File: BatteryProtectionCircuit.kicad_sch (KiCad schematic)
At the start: 0 parts

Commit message: Added initial power supply and wiring
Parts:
- added R1: R_US, symbol Device:R_US
- added U1: LMC555xN, Package_DIP:DIP-8_W7.62mm, symbol Timer:LMC555xN
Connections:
- new net: R1.2, U1.7 (DIS)
- new net +5V: U1.8 (VCC)

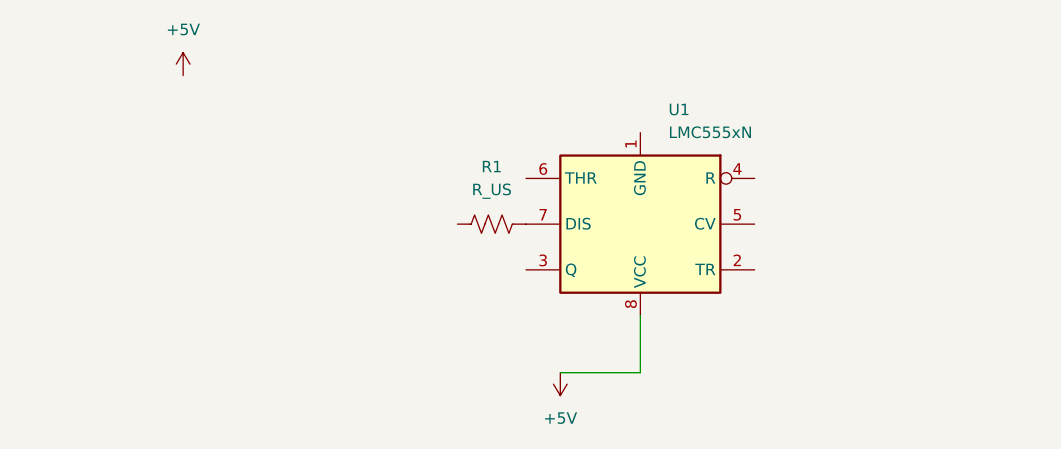
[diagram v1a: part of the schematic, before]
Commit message: BPC timer module complete (for 1 cell)
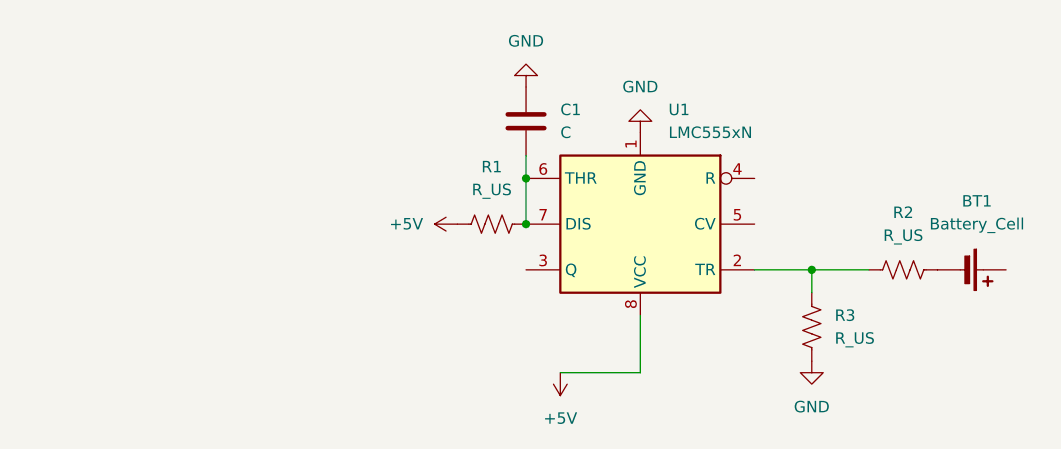
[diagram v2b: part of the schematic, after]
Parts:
- added BT1: Battery_Cell, symbol Device:Battery_Cell
- added C1: C, symbol Device:C
- added R2, R3: R_US, symbol Device:R_US
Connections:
- net +5V: now also R1.1
- net at R1.2, U1.7 (DIS): now also U1.6 (THR), C1.2
- net GND: now reaches U1.1 (GND)
- net GND: now also C1.1, R3.2
- net at U1.2 (TR): now also R2.1, R3.1
- new net: BT1.2 (-), R2.2

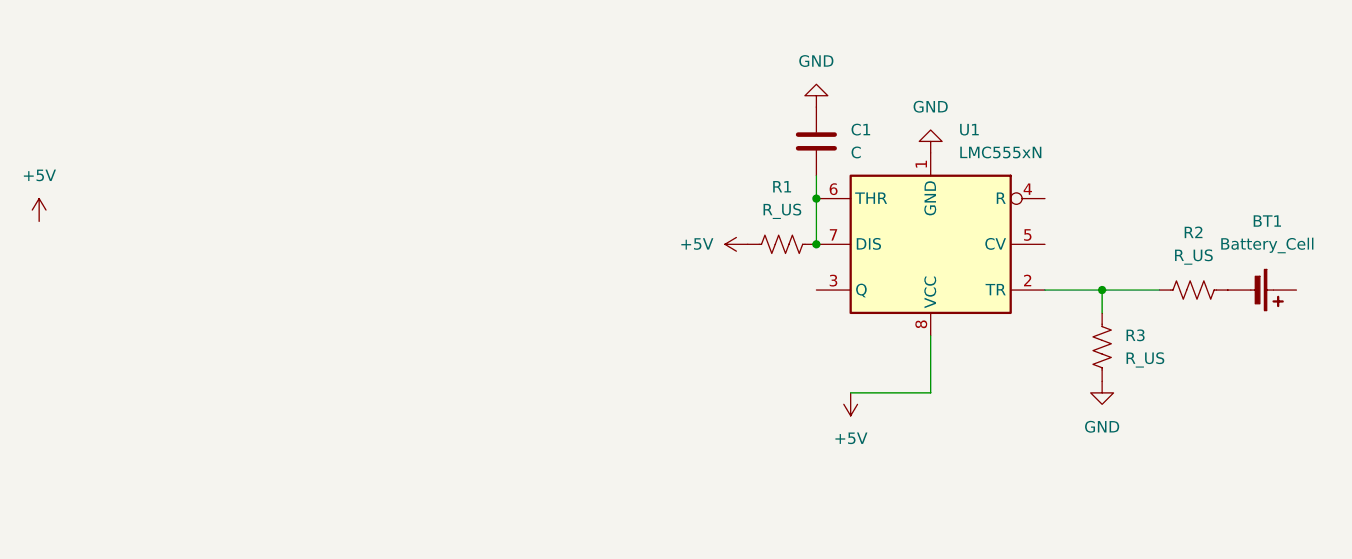
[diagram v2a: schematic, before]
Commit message: Finished 555 based Protection Circuit for Singular Cell
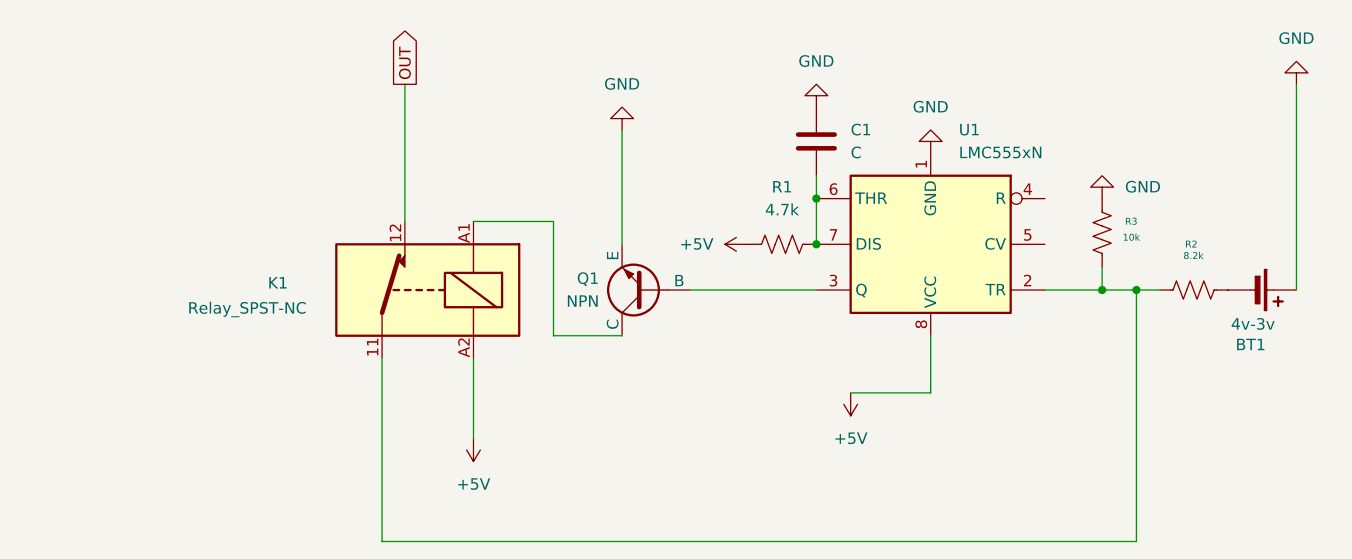
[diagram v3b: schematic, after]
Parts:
- added K1: Relay_SPST-NC, symbol Relay:Relay_SPST-NC
- added Q1: NPN, symbol Simulation_SPICE:NPN
- BT1: value Battery_Cell -> 4v-3v
- R1: value R_US -> 4.7k
- R2: value R_US -> 8.2k
- R3: value R_US -> 10k
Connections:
- net +5V: now also K1.A2
- net GND: now also BT1.1 (+), R3.1, Q1.3 (E); no longer R3.2
- net at R2.1, U1.2 (TR): now also R3.2, K1.11; no longer R3.1
- net at U1.3 (Q): now also Q1.2 (B)
- new net: K1.A1, Q1.1 (C)
- new net OUT: K1.12
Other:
- moved on the sheet: R3

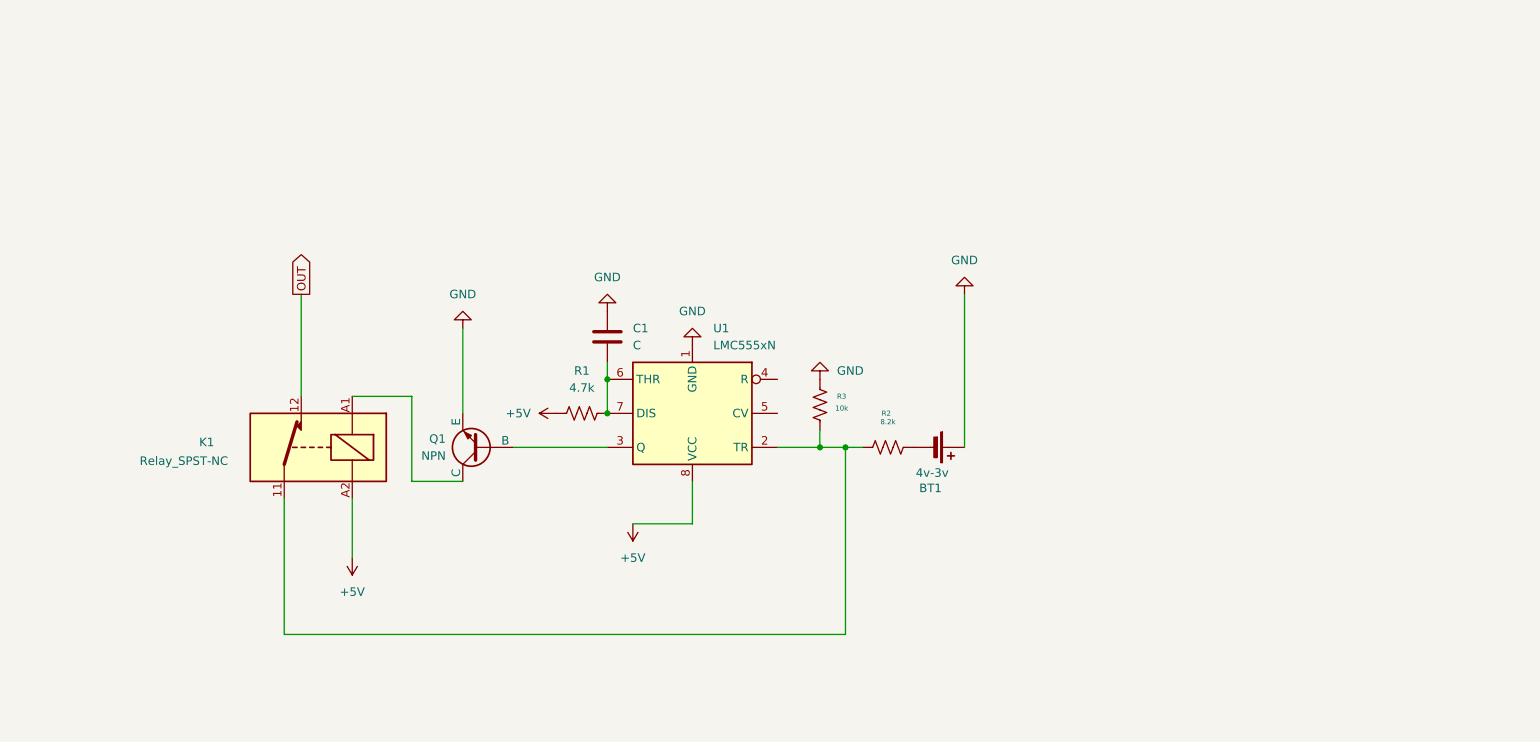
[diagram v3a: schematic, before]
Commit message: Added Flyback Diode to Relay to Prevent Voltage Spiking
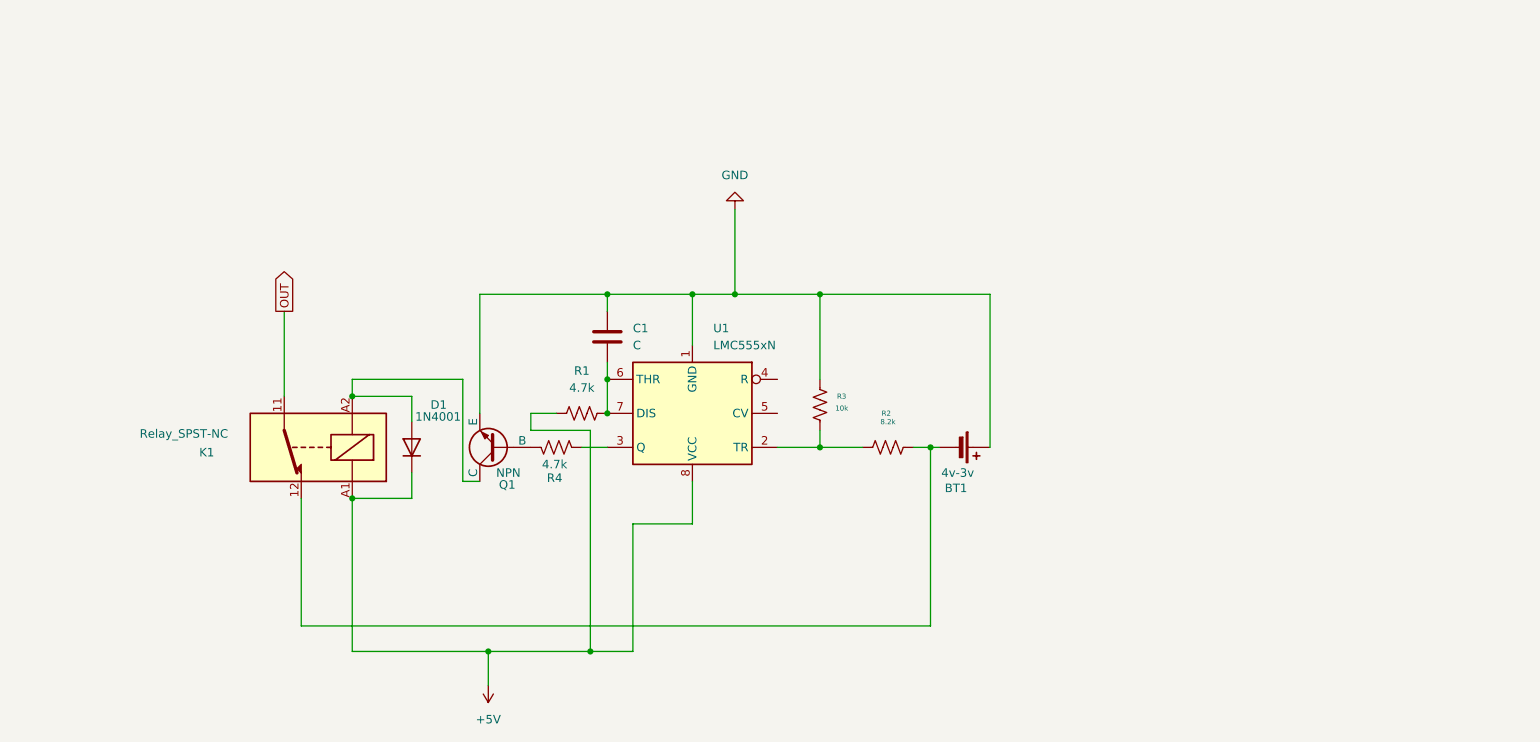
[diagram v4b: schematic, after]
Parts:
- added D1: 1N4001, Diode_THT:D_DO-41_SOD81_P10.16mm_Horizontal, symbol Diode:1N4001
- added R4: 4.7k, symbol Device:R_US
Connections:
- net +5V: now also K1.A1, D1.1 (K); no longer K1.A2
- net OUT: now also K1.11; no longer K1.12
- net at Q1.1 (C): now also K1.A2, D1.2 (A); no longer K1.A1
- net at Q1.2 (B): now also R4.2; no longer U1.3 (Q)
- net at R2.1, R3.2, U1.2 (TR): no longer K1.11
- net at BT1.2 (-), R2.2: now also K1.12
- new net: R4.1, U1.3 (Q)
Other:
- moved on the sheet: BT1, K1, Q1

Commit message: Added op-amps and diode-and network to filter out smallest voltage out of all battery cells
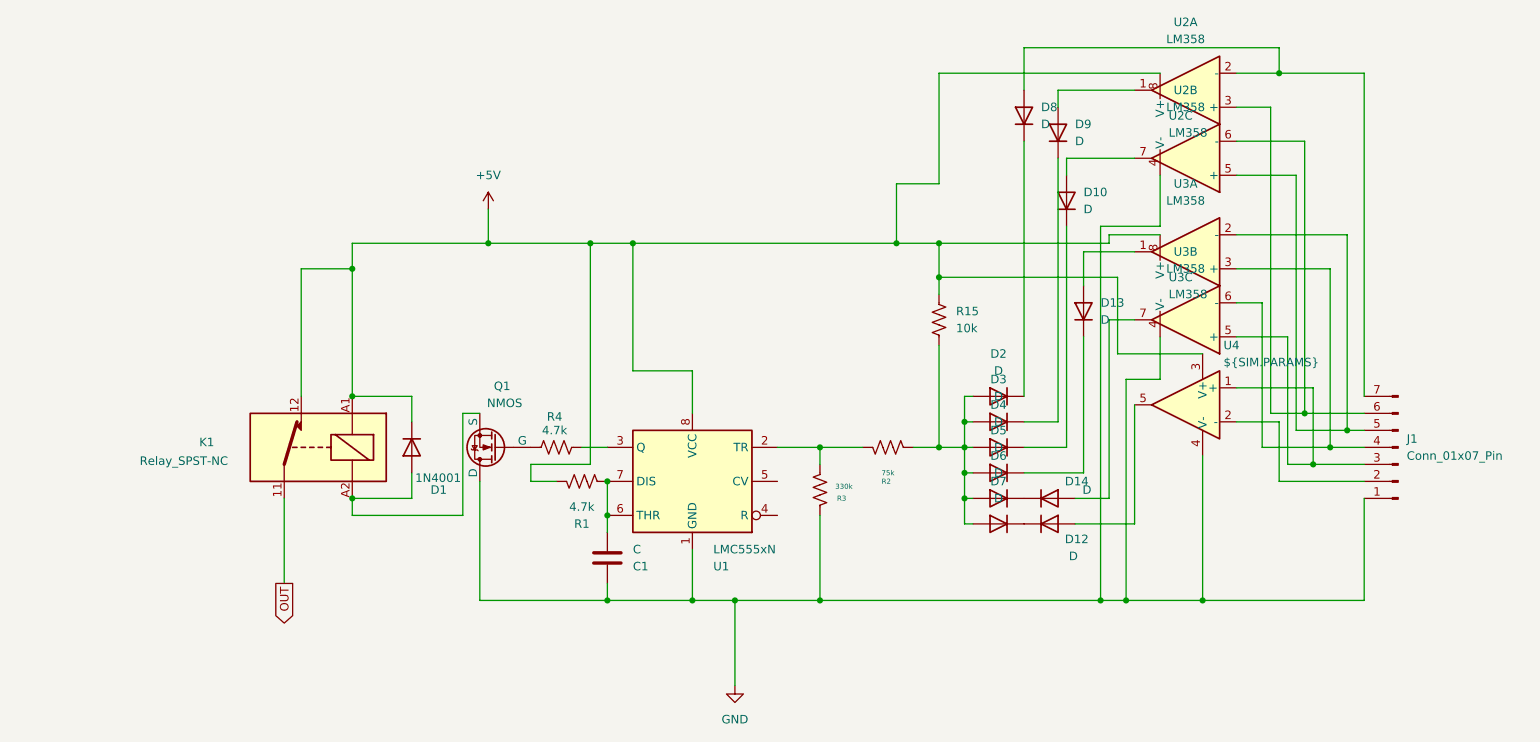
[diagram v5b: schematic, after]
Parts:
- removed BT1: 4v-3v, symbol Device:Battery_Cell
- removed Q1: NPN, symbol Simulation_SPICE:NPN
- added D10, D12, D13, D14, D2, D3, D4, D5, D6, D7, D8, D9: D, symbol Device:D
- added J1: Conn_01x07_Pin, Connector_JST:JST_XH_B7B-XH-AM_1x07_P2.50mm_Vertical, symbol Connector:Conn_01x07_Pin
- added Q1: NMOS, symbol Simulation_SPICE:NMOS
- added R15: 10k, symbol Device:R_US
- added U2, U3: LM358, symbol Amplifier_Operational:LM358
- added U4: ${SIM.PARAMS}, symbol Simulation_SPICE:OPAMP
- R2: value 8.2k -> 75k
- R3: value 10k -> 330k
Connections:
- net +5V: now also K1.12, R15.1, U2.8 (V+), U3.8 (V+), U4.3 (V+)
- net GND: now also J1.1 (Pin_1), Q1.1 (D), U2.4 (V-), U3.4 (V-), U4.4 (V-)
- net at D1.2 (A), K1.A2: now also Q1.3 (S)
- net at R4.2: now also Q1.2 (G)
- net at R2.2: now also D2.2 (A), D3.2 (A), D4.2 (A), D5.2 (A), D6.2 (A), D7.2 (A), R15.2; no longer K1.12
- new net: J1.3 (Pin_3), U3.5 (+), U4.1 (+)
- new net: J1.4 (Pin_4), U3.3 (+), U3.6 (-)
- new net: D14.2 (A), U3.7
- new net: D14.1 (K), D6.1 (K)
- new net: J1.5 (Pin_5), U2.5 (+), U3.2 (-)
- new net: J1.6 (Pin_6), U2.3 (+), U2.6 (-)
- new net: D10.2 (A), U2.7
- new net: J1.2 (Pin_2), U4.2 (-)
- new net: D8.2 (A), J1.7 (Pin_7), U2.2 (-)
- new net: D12.2 (A), U4.5
- new net: D2.1 (K), D8.1 (K)
- new net: D13.1 (K), D5.1 (K)
- new net: D13.2 (A), U3.1
- new net: D10.1 (K), D4.1 (K)
- new net: D12.1 (K), D7.1 (K)
- new net: D3.1 (K), D9.1 (K)
- new net: D9.2 (A), U2.1
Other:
- moved on the sheet: C1, K1, R1, R3, U1
